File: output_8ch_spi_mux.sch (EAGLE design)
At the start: 49 parts, among them IC1 TPS706-1V8, IC2 5M160ZE64, IC3 SN75174SOIC-20, IC4 SN75174SOIC-20, IC6 STM32F042F, IC7 CAT24C256, Q1 50MHz

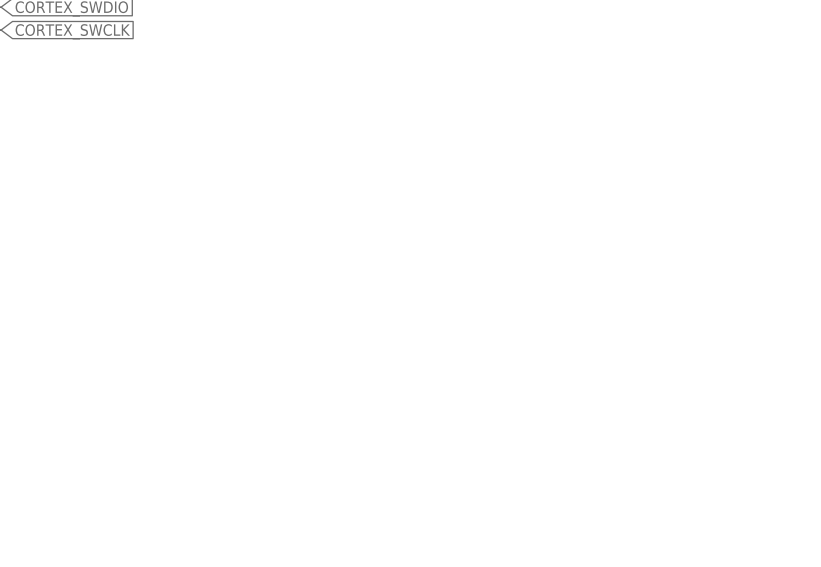
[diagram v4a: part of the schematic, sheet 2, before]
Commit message: Added cortex debug header
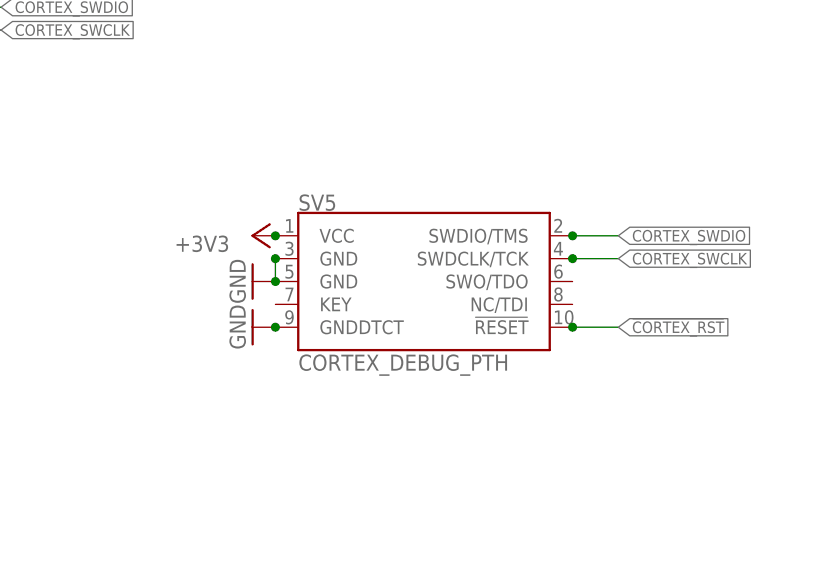
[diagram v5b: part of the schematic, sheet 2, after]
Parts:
- added SV5: CORTEX_DEBUG_PTH, lichtenstein_onion:CORTEX_DEBUG_PTH
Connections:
- net !CORTEX_RST: now also SV5.!RESET
- net +3V3: now also SV5.VCC
- net CORTEX_SWCLK: now also SV5.SWDCLK/TCK
- net CORTEX_SWDIO: now also SV5.SWDIO/TMS
- net GND: now also SV5.GND@3, SV5.GND@5, SV5.GNDDTCT
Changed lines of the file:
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@@
 <part name="SV4" library="con-lstb" library_urn="urn:adsk.eagle:library:162" deviceset="MA03-1" device="" package3d_urn="urn:adsk.eagle:package:8339/1"/>
 <part name="GND36" library="supply1" library_urn="urn:adsk.eagle:library:371" deviceset="GND" device=""/>
+<part name="SV5" library="lichtenstein_onion" deviceset="CORTEX_DEBUG" device="_PTH"/>
+<part name="GND37" library="supply1" library_urn="urn:adsk.eagle:library:371" deviceset="GND" device=""/>
+<part name="GND38" library="supply1" library_urn="urn:adsk.eagle:library:371" deviceset="GND" device=""/>
+<part name="+3V4" library="supply1" library_urn="urn:adsk.eagle:library:371" deviceset="+3V3" device=""/>
 </parts>
 <sheets>
@@
 <attribute name="VALUE" x="127" y="55.88" size="1.778" layer="96"/>
 </instance>
+<instance part="SV5" gate="G$1" x="205.74" y="73.66" smashed="yes">
+<attribute name="NAME" x="193.04" y="81.534" size="1.778" layer="95" font="vector"/>
+<attribute name="VALUE" x="193.04" y="63.754" size="1.778" layer="96" font="vector"/>
+</instance>
+<instance part="GND37" gate="1" x="187.96" y="68.58" smashed="yes" rot="R270">
+<attribute name="VALUE" x="185.42" y="71.12" size="1.778" layer="96" rot="R270"/>
+</instance>
+<instance part="GND38" gate="1" x="187.96" y="73.66" smashed="yes" rot="R270">
+<attribute name="VALUE" x="185.42" y="76.2" size="1.778" layer="96" rot="R270"/>
+</instance>
+<instance part="+3V4" gate="G$1" x="187.96" y="78.74" smashed="yes" rot="R90">
+<attribute name="VALUE" x="185.42" y="78.74" size="1.778" layer="96" rot="R180"/>
+</instance>
 </instances>
 <busses>
@@
 <junction x="129.54" y="60.96"/>
 </segment>
+<segment>
+<pinref part="SV5" gate="G$1" pin="GNDDTCT"/>
+<pinref part="GND37" gate="1" pin="GND"/>
+<junction x="190.5" y="68.58"/>
+</segment>
+<segment>
+<pinref part="SV5" gate="G$1" pin="GND@5"/>
+<pinref part="GND38" gate="1" pin="GND"/>
+<pinref part="SV5" gate="G$1" pin="GND@3"/>
+<wire x1="190.5" y1="76.2" x2="190.5" y2="73.66" width="0.1524" layer="91"/>
+<junction x="190.5" y="76.2"/>
+<junction x="190.5" y="73.66"/>
+</segment>
 </net>
 <net name="+3V3" class="0">
@@
 <junction x="116.84" y="101.6"/>
 </segment>
+<segment>
+<pinref part="SV5" gate="G$1" pin="VCC"/>
+<pinref part="+3V4" gate="G$1" pin="+3V3"/>
+<junction x="190.5" y="78.74"/>
+</segment>
 </net>
 <net name="ID_SCL" class="0">
@@
 <junction x="116.84" y="132.08"/>
 </segment>
+<segment>
+<pinref part="SV5" gate="G$1" pin="!RESET"/>
+<wire x1="223.52" y1="68.58" x2="228.6" y2="68.58" width="0.1524" layer="91"/>
+<label x="228.6" y="68.58" size="1.27" layer="95" xref="yes"/>
+<junction x="223.52" y="68.58"/>
+</segment>
 </net>
 <net name="CORTEX_SWDIO" class="0">
@@
 <junction x="154.94" y="104.14"/>
 </segment>
+<segment>
+<pinref part="SV5" gate="G$1" pin="SWDIO/TMS"/>
+<wire x1="223.52" y1="78.74" x2="228.6" y2="78.74" width="0.1524" layer="91"/>
+<label x="228.6" y="78.74" size="1.27" layer="95" xref="yes"/>
+<junction x="223.52" y="78.74"/>
+</segment>
 </net>
 <net name="CORTEX_SWCLK" class="0">
@@
 <junction x="154.94" y="101.6"/>
 </segment>
-</net>
+<segment>
+<pinref part="SV5" gate="G$1" pin="SWDCLK/TCK"/>
+<wire x1="223.52" y1="76.2" x2="228.6" y2="76.2" width="0.1524" layer="91"/>
+<label x="228.6" y="76.2" size="1.27" layer="95" xref="yes"/>
+<junction x="223.52" y="76.2"/>
+</segment>
+</net>

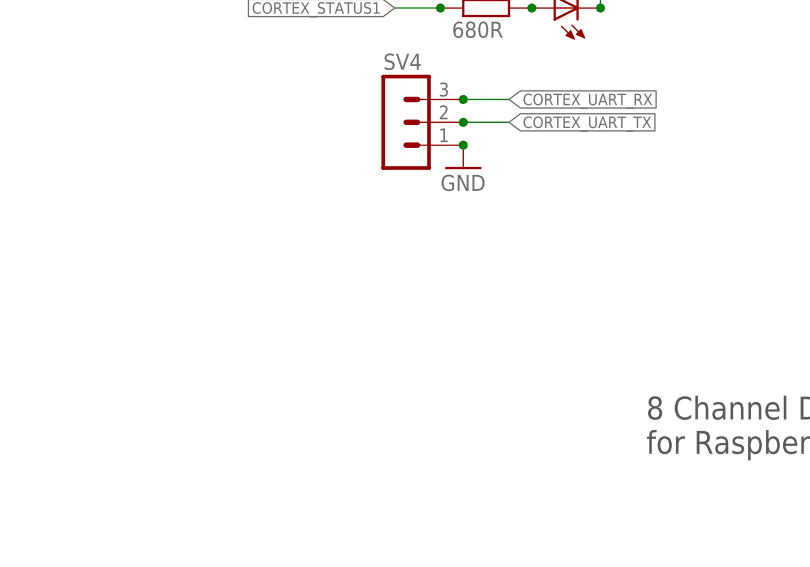
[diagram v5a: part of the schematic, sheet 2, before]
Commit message: Added I2C testpoints
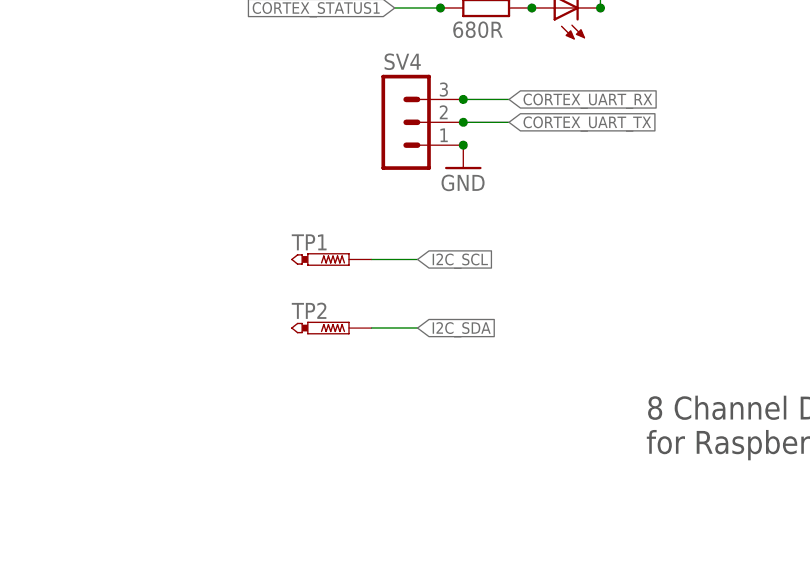
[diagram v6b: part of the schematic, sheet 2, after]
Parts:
- added TP1, TP2: PTR1B1,27, testpad:PTR1B1,27
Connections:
- net I2C_SCL: now also TP1.TP
- net I2C_SDA: now also TP2.TP
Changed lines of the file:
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@@
 <part name="GND38" library="supply1" library_urn="urn:adsk.eagle:library:371" deviceset="GND" device=""/>
 <part name="+3V4" library="supply1" library_urn="urn:adsk.eagle:library:371" deviceset="+3V3" device=""/>
+<part name="TP1" library="testpad" library_urn="urn:adsk.eagle:library:385" deviceset="PTR1" device="B1,27" package3d_urn="urn:adsk.eagle:package:27944/1"/>
+<part name="TP2" library="testpad" library_urn="urn:adsk.eagle:library:385" deviceset="PTR1" device="B1,27" package3d_urn="urn:adsk.eagle:package:27944/1"/>
 </parts>
 <sheets>
@@
 <wire x1="73.66" y1="88.9" x2="68.58" y2="88.9" width="0.1524" layer="91"/>
 <label x="68.58" y="88.9" size="1.27" layer="95" rot="R180" xref="yes"/>
+<junction x="73.66" y="88.9"/>
 </segment>
 </net>
@@
 <wire x1="73.66" y1="99.06" x2="68.58" y2="99.06" width="0.1524" layer="91"/>
 <label x="68.58" y="99.06" size="1.27" layer="95" rot="R180" xref="yes"/>
+<junction x="73.66" y="99.06"/>
 </segment>
 </net>
@@
 <wire x1="68.58" y1="96.52" x2="73.66" y2="96.52" width="0.1524" layer="91"/>
 <label x="68.58" y="96.52" size="1.27" layer="95" rot="R180" xref="yes"/>
+<junction x="73.66" y="96.52"/>
 </segment>
 </net>
@@
 <wire x1="73.66" y1="93.98" x2="68.58" y2="93.98" width="0.1524" layer="91"/>
 <label x="68.58" y="93.98" size="1.27" layer="95" rot="R180" xref="yes"/>
+<junction x="73.66" y="93.98"/>
 </segment>
 </net>
@@
 <wire x1="73.66" y1="91.44" x2="68.58" y2="91.44" width="0.1524" layer="91"/>
 <label x="68.58" y="91.44" size="1.27" layer="95" rot="R180" xref="yes"/>
+<junction x="73.66" y="91.44"/>
 </segment>
 </net>
@@
 <wire x1="73.66" y1="137.16" x2="68.58" y2="137.16" width="0.1524" layer="91"/>
 <label x="68.58" y="137.16" size="1.27" layer="95" rot="R180" xref="yes"/>
+<junction x="73.66" y="137.16"/>
 </segment>
 </net>
@@
 <wire x1="73.66" y1="139.7" x2="68.58" y2="139.7" width="0.1524" layer="91"/>
 <label x="68.58" y="139.7" size="1.27" layer="95" rot="R180" xref="yes"/>
+<junction x="73.66" y="139.7"/>
 </segment>
 </net>
@@
 <wire x1="73.66" y1="142.24" x2="68.58" y2="142.24" width="0.1524" layer="91"/>
 <label x="68.58" y="142.24" size="1.27" layer="95" rot="R180" xref="yes"/>
+<junction x="73.66" y="142.24"/>
 </segment>
 </net>
@@
 <wire x1="73.66" y1="144.78" x2="68.58" y2="144.78" width="0.1524" layer="91"/>
 <label x="68.58" y="144.78" size="1.27" layer="95" rot="R180" xref="yes"/>
+<junction x="73.66" y="144.78"/>
 </segment>
 </net>
@@
 <attribute name="VALUE" x="185.42" y="78.74" size="1.778" layer="96" rot="R180"/>
 </instance>
+<instance part="TP1" gate="G$1" x="116.84" y="48.26" smashed="yes" rot="R270">
+<attribute name="NAME" x="110.49" y="49.276" size="1.778" layer="95"/>
+<attribute name="TP_SIGNAL_NAME" x="114.3" y="46.99" size="1.778" layer="97" rot="R270"/>
+</instance>
+<instance part="TP2" gate="G$1" x="116.84" y="40.64" smashed="yes" rot="R270">
+<attribute name="NAME" x="110.49" y="41.656" size="1.778" layer="95"/>
+<attribute name="TP_SIGNAL_NAME" x="114.3" y="39.37" size="1.778" layer="97" rot="R270"/>
+</instance>
 </instances>
 <busses>
@@
 <junction x="116.84" y="121.92"/>
 </segment>
+<segment>
+<wire x1="119.38" y1="40.64" x2="124.46" y2="40.64" width="0.1524" layer="91"/>
+<label x="124.46" y="40.64" size="1.27" layer="95" xref="yes"/>
+<pinref part="TP2" gate="G$1" pin="TP"/>
+</segment>
 </net>
 <net name="I2C_SCL" class="0">
@@
 <junction x="116.84" y="119.38"/>
 </segment>
-</net>
+<segment>
+<wire x1="124.46" y1="48.26" x2="119.38" y2="48.26" width="0.1524" layer="91"/>
+<label x="124.46" y="48.26" size="1.27" layer="95" xref="yes"/>
+<pinref part="TP1" gate="G$1" pin="TP"/>
+</segment>
+</net>

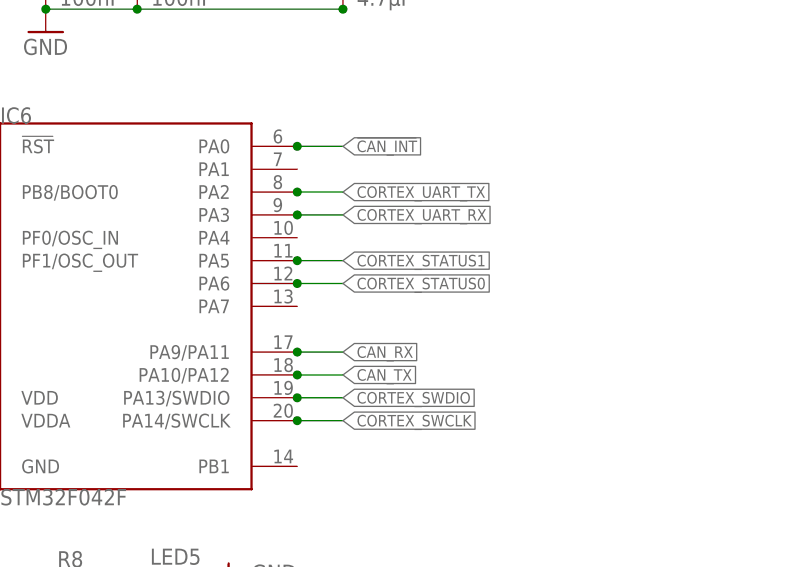
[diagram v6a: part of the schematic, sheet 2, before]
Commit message: Added clock calibration signal to cannabus controller (divide 50MHz clk by 1000 in CPLD)
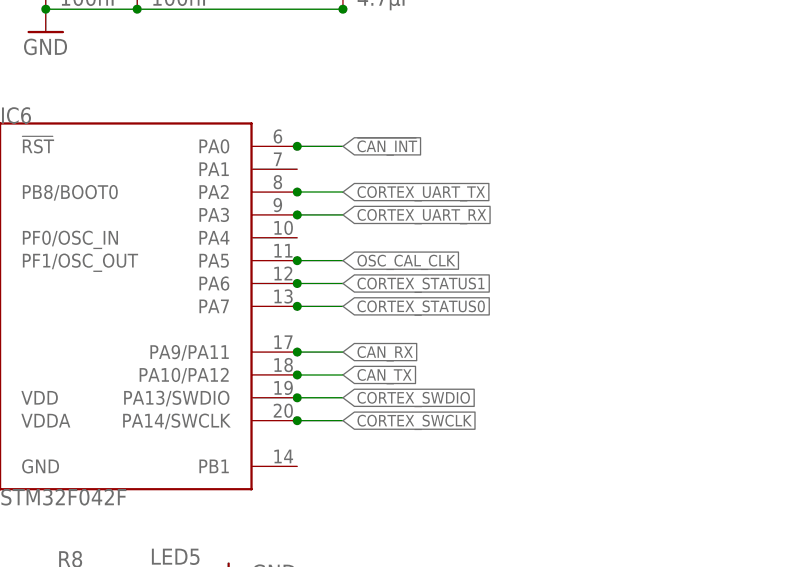
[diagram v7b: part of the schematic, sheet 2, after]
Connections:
- new net OSC_CAL_CLK: IC2.IO49, IC6.PA5
- net CORTEX_STATUS0: now also IC6.PA7; no longer IC6.PA6
- net CORTEX_STATUS1: now also IC6.PA6; no longer IC6.PA5
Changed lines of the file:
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@@
+</segment>
+</net>
+<net name="OSC_CAL_CLK" class="0">
+<segment>
+<pinref part="IC2" gate="G$1" pin="IO49"/>
+<wire x1="109.22" y1="121.92" x2="114.3" y2="121.92" width="0.1524" layer="91"/>
+<label x="114.3" y="121.92" size="1.27" layer="95" xref="yes"/>
+<junction x="109.22" y="121.92"/>
 </segment>
 </net>
@@
 </segment>
 <segment>
+<pinref part="IC6" gate="G$1" pin="PA6"/>
+<wire x1="154.94" y1="116.84" x2="160.02" y2="116.84" width="0.1524" layer="91"/>
+<label x="160.02" y="116.84" size="1.27" layer="95" xref="yes"/>
+<junction x="154.94" y="116.84"/>
+</segment>
+</net>
+<net name="CORTEX_STATUS0" class="0">
+<segment>
+<pinref part="R8" gate="G$1" pin="1"/>
+<wire x1="127" y1="83.82" x2="121.92" y2="83.82" width="0.1524" layer="91"/>
+<label x="121.92" y="83.82" size="1.27" layer="95" rot="R180" xref="yes"/>
+<junction x="127" y="83.82"/>
+</segment>
+<segment>
+<pinref part="IC6" gate="G$1" pin="PA7"/>
+<wire x1="154.94" y1="114.3" x2="160.02" y2="114.3" width="0.1524" layer="91"/>
+<label x="160.02" y="114.3" size="1.27" layer="95" xref="yes"/>
+<junction x="154.94" y="114.3"/>
+</segment>
+</net>
+<net name="N$5" class="0">
+<segment>
+<pinref part="LED6" gate="G$1" pin="A"/>
+<pinref part="R9" gate="G$1" pin="2"/>
+<junction x="137.16" y="76.2"/>
+</segment>
+</net>
+<net name="OSC_CAL_CLK" class="0">
+<segment>
 <pinref part="IC6" gate="G$1" pin="PA5"/>
 <wire x1="154.94" y1="119.38" x2="160.02" y2="119.38" width="0.1524" layer="91"/>
@@
 </segment>
 </net>
-<net name="CORTEX_STATUS0" class="0">
-<segment>
-<pinref part="R8" gate="G$1" pin="1"/>
-<wire x1="127" y1="83.82" x2="121.92" y2="83.82" width="0.1524" layer="91"/>
-<label x="121.92" y="83.82" size="1.27" layer="95" rot="R180" xref="yes"/>
-<junction x="127" y="83.82"/>
-</segment>
-<segment>
-<pinref part="IC6" gate="G$1" pin="PA6"/>
-<wire x1="154.94" y1="116.84" x2="160.02" y2="116.84" width="0.1524" layer="91"/>
-<label x="160.02" y="116.84" size="1.27" layer="95" xref="yes"/>
-<junction x="154.94" y="116.84"/>
-</segment>
-</net>
-<net name="N$5" class="0">
-<segment>
-<pinref part="LED6" gate="G$1" pin="A"/>
-<pinref part="R9" gate="G$1" pin="2"/>
-<junction x="137.16" y="76.2"/>
-</segment>
-</net>

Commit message: yes
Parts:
- LED5, LED6: value (none) -> GRN
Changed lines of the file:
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@@
 <part name="GND6" library="supply1" library_urn="urn:adsk.eagle:library:371" deviceset="GND" device=""/>
 <part name="+3V33" library="supply1" library_urn="urn:adsk.eagle:library:371" deviceset="+3V3" device=""/>
-<part name="IC5" library="lichtenstein_onion" deviceset="TXB0108" device="TSSOP20"/>
+<part name="IC5" library="lichtenstein_onion" deviceset="TXB0108" device="TSSOP20" package3d_urn="urn:adsk.eagle:package:4349/2"/>
 <part name="+3V38" library="supply1" library_urn="urn:adsk.eagle:library:371" deviceset="+3V3" device=""/>
 <part name="GND17" library="supply1" library_urn="urn:adsk.eagle:library:371" deviceset="GND" device=""/>
@@
 </part>
 <part name="GND15" library="supply1" library_urn="urn:adsk.eagle:library:371" deviceset="GND" device=""/>
-<part name="IC1" library="lichtenstein_onion" deviceset="TPS706" device="SOT23-5" value="TPS706-1V8"/>
+<part name="IC1" library="lichtenstein_onion" deviceset="TPS706" device="SOT23-5" package3d_urn="urn:adsk.eagle:package:16456/2" value="TPS706-1V8"/>
 <part name="+3V32" library="supply1" library_urn="urn:adsk.eagle:library:371" deviceset="+3V3" device=""/>
 <part name="GND7" library="supply1" library_urn="urn:adsk.eagle:library:371" deviceset="GND" device=""/>
@@
 <attribute name="MOUSER" value="710-885012207072"/>
 </part>
-<part name="IC6" library="lichtenstein_onion" deviceset="STM32F042F" device=""/>
-<part name="LED5" library="led" library_urn="urn:adsk.eagle:library:259" deviceset="LED" device="CHIPLED_1206" package3d_urn="urn:adsk.eagle:package:15823/2">
+<part name="IC6" library="lichtenstein_onion" deviceset="STM32F042F" device="" package3d_urn="urn:adsk.eagle:package:4349/2"/>
+<part name="LED5" library="led" library_urn="urn:adsk.eagle:library:259" deviceset="LED" device="CHIPLED_1206" package3d_urn="urn:adsk.eagle:package:15823/2" value="GRN">
 <attribute name="MOUSER" value="604-APTR3216SGC"/>
 </part>
@@
 <attribute name="MOUSER" value="652-CR0805-FX6800GLF"/>
 </part>
-<part name="LED6" library="led" library_urn="urn:adsk.eagle:library:259" deviceset="LED" device="CHIPLED_1206" package3d_urn="urn:adsk.eagle:package:15823/2">
+<part name="LED6" library="led" library_urn="urn:adsk.eagle:library:259" deviceset="LED" device="CHIPLED_1206" package3d_urn="urn:adsk.eagle:package:15823/2" value="GRN">
 <attribute name="MOUSER" value="604-APTR3216SGC"/>
 </part>
@@
 <attribute name="MOUSER" x="139.7" y="83.82" size="1.27" layer="96" rot="R90" align="top-center" display="off"/>
 <attribute name="NAME" x="144.272" y="87.376" size="1.778" layer="95" rot="R180"/>
-<attribute name="VALUE" x="144.272" y="89.535" size="1.778" layer="96" rot="R180"/>
+<attribute name="VALUE" x="151.892" y="86.995" size="1.778" layer="96" rot="R180"/>
 </instance>
 <instance part="R8" gate="G$1" x="132.08" y="83.82" smashed="yes">
@@
 <attribute name="MOUSER" x="139.7" y="76.2" size="1.27" layer="96" rot="R90" align="top-center" display="off"/>
 <attribute name="NAME" x="144.272" y="79.756" size="1.778" layer="95" rot="R180"/>
-<attribute name="VALUE" x="144.272" y="81.915" size="1.778" layer="96" rot="R180"/>
+<attribute name="VALUE" x="151.892" y="79.375" size="1.778" layer="96" rot="R180"/>
 </instance>
 <instance part="GND35" gate="1" x="114.3" y="127" smashed="yes" rot="R270">
